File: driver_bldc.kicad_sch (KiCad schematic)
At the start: 1 part, among them U1 STM32G431CBT6

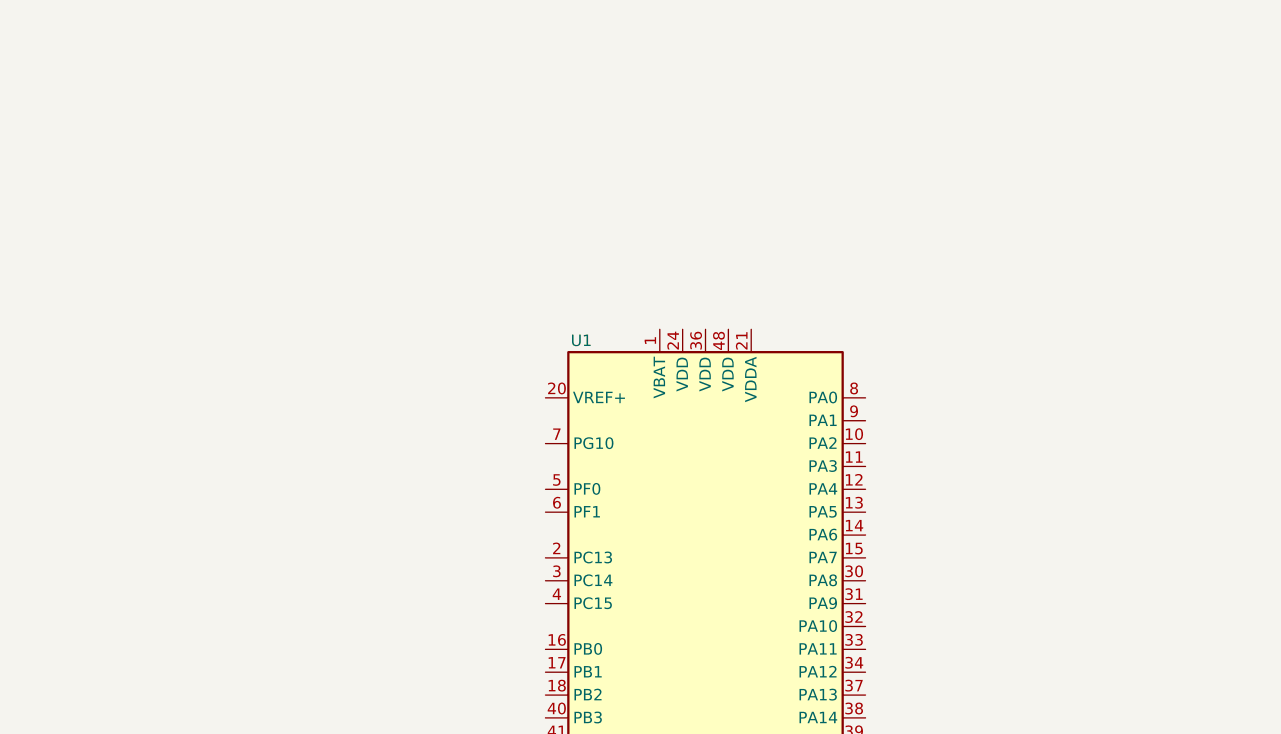
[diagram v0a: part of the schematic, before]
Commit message: dodati decoupling C i NRST
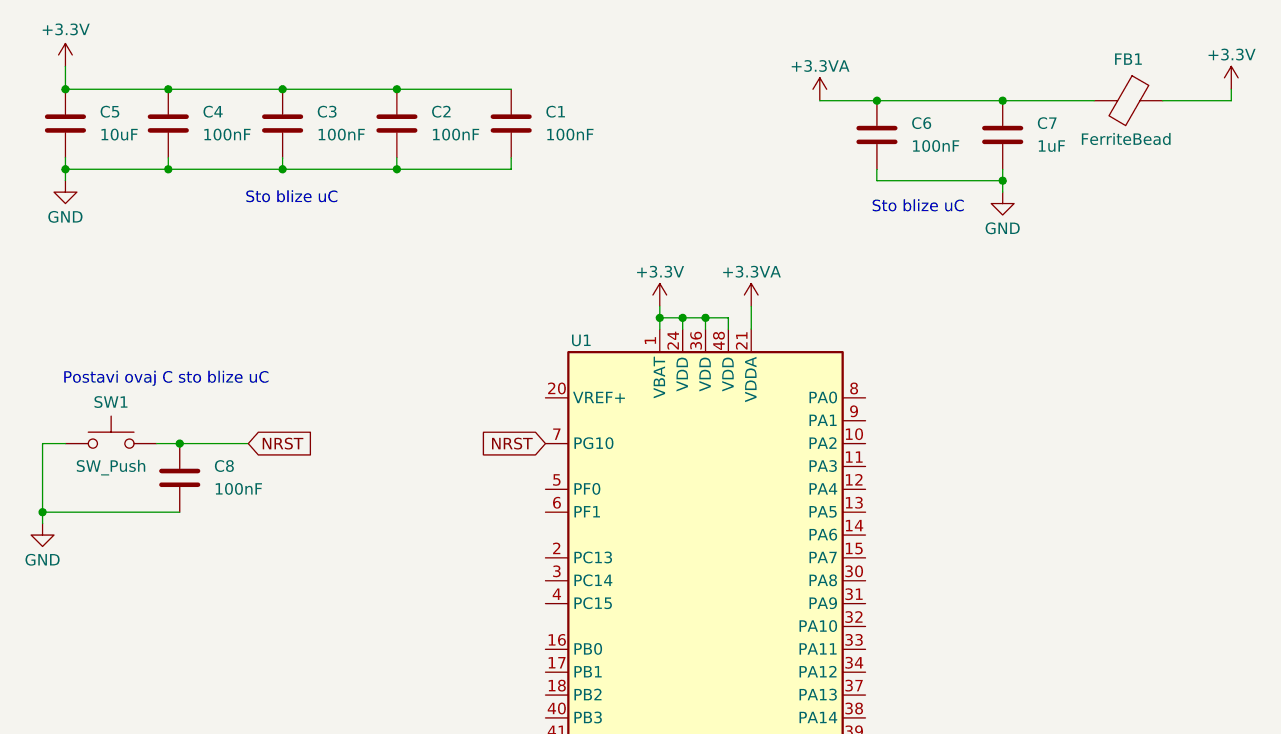
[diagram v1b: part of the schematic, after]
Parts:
- added C1, C2, C3, C4, C6, C8: 100nF, symbol Device:C
- added C5: 10uF, symbol Device:C
- added C7: 1uF, symbol Device:C
- added FB1: FerriteBead, symbol Device:FerriteBead
- added SW1: SW_Push, symbol Switch:SW_Push
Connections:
- net GND: now also C1.2, C2.2, C3.2, C4.2, C5.2, C6.2, C7.2, C8.2, SW1.1
- net +3.3V: now reaches U1.1 (VBAT)
- net +3.3V: now also U1.24 (VDD), U1.36 (VDD), U1.48 (VDD), C1.1, C2.1, C3.1, C4.1, C5.1, FB1.1
- net +3.3VA: now reaches U1.21 (VDDA)
- net +3.3VA: now also C6.1, C7.1, FB1.2
- net NRST: now reaches U1.7 (PG10)
- net NRST: now also C8.1, SW1.2
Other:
- note added: "Postavi ovaj C sto blize uC"
- note added: "Sto blize uC"

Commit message: CAN dodat
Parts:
- added C10, C9: 10pF, symbol Device:C
- added C11: 100nF, symbol Device:C
- added C12: 4.7nF, symbol Device:C
- added J1: Conn_01x03, Connector_Molex:Molex_SPOX_5267-03A_1x03_P2.50mm_Vertical, symbol Connector_Generic:Conn_01x03
- added Q1, Q2, Q3: BTN8982TA, Package_TO_SOT_SMD:TO-263-7_TabPin8, symbol Power_Management:BTN8982TA
- added R1: 0, symbol Device:R
- added R2: 10k, symbol Device:R
- added R3: 330, symbol Device:R
- added R4, R5: 60, symbol Device:R
- added U2: SN65HVD234, Package_SO:SOIC-8_3.9x4.9mm_P1.27mm, symbol Interface_CAN_LIN:SN65HVD234
- added Y1: 16MHz, symbol Device:Crystal_GND24
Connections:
- net +3.3V: now also C11.1, U2.3 (VCC)
- net GND: now also C10.2, C11.2, C12.2, C9.2, J1.1 (Pin_1), R2.1, U2.2 (GND), U2.8 (Rs), Y1.2, Y1.4
- net CAN_EN: now reaches U1.30 (PA8)
- net CAN_EN: now also R3.1
- net CAN_RX: now reaches U1.33 (PA11)
- net CAN_RX: now also U2.4 (R)
- net CAN_TX: now reaches U1.34 (PA12)
- net CAN_TX: now also U2.1 (D)
- net SW_DIO: now reaches U1.37 (PA13)
- net SW_CLK: now reaches U1.38 (PA14)
- net BOOT0: now reaches U1.45 (PB8)
- net BOOT0: now also R2.2
- net HSE_IN: now reaches U1.5 (PF0)
- net HSE_IN: now also C10.1, Y1.1
- net HSE_OUT: now reaches U1.6 (PF1)
- net HSE_OUT: now also R1.1
- new net: C12.1, R4.2, R5.1
- new net: Q2.4, Q2.8
- new net: C9.1, R1.2, Y1.3
- new net: R3.2, U2.5 (EN)
- new net: Q3.4, Q3.8
- new net: Q1.4, Q1.8
- new net CANH: J1.2 (Pin_2), R4.1, U2.7 (CANH)
- new net CANL: J1.3 (Pin_3), R5.2, U2.6 (CANL)
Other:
- note added: "CAN Transceiver"
- note added: "Cload = 2 * (CL - Cstray) = 2 * (9pF - 5pF) = 8pF --> 10pF"
- note added: "Ovo se dodaje samo na krajevima CAN magistrale?"
- note added: "STM32G431CBT6"
- moved on the sheet: C1, C2, C3, C4, C5, C6, C7, C8, FB1, SW1, U1

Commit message: dodat buck
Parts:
- added C13: 10uF, symbol Device:C
- added C14: 100nF, symbol Device:C
- added C15, C16: 22uF, symbol Device:C
- added J2: SWD, symbol Connector:Conn_01x10_Pin
- added J3: BATT, Connector_AMASS:AMASS_XT30PW-M_1x02_P2.50mm_Horizontal, symbol Connector_Generic:Conn_01x02
- added L1: 3.9uH, symbol Device:L
- added U3: AP63203WU, Package_TO_SOT_SMD:TSOT-23-6_HandSoldering, symbol Regulator_Switching:AP63203WU
- J1: value Conn_01x03 -> CAN
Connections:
- net +3.3V: now also C15.1, C16.1, J2.1 (Pin_1), L1.2, U3.1 (FB)
- net GND: now also C13.2, C15.2, C16.2, J2.3 (Pin_3), J2.5 (Pin_5), J2.9 (Pin_9), J3.2 (Pin_2), U3.4 (GND)
- net NRST: now also J2.10 (Pin_10)
- net SW_CLK: now also J2.4 (Pin_4)
- net SW_DIO: now also J2.2 (Pin_2)
- net B: now reaches Q2.4, Q2.8
- net C: now reaches Q3.4, Q3.8
- net A: now reaches Q1.4, Q1.8
- net CAN_RX renamed CAN_RX+
- net CAN_TX renamed CAN_TX-
- new net: C14.1, L1.1, U3.5 (SW)
- new net: C14.2, U3.6 (BST)
- new net +24V: C13.1, J3.1 (Pin_1), U3.2 (EN), U3.3 (IN)
- no-connect marks 0 -> 3
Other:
- note added: "Buck converter"
- moved on the sheet: C1, C10, C2, C3, C4, C5, C6, C7, C8, C9, FB1, Q1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
